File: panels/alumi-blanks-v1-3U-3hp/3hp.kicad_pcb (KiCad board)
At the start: 2 copper layers, 14.9 x 128.5 mm, 2 parts

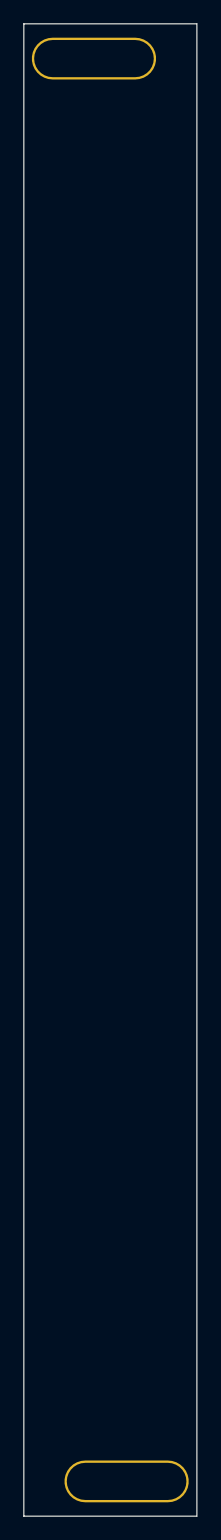
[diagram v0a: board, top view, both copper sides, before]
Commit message: feat: add new screw hole footprints and update panel KiCad files for new JLCPCB order
- Added modular-3M-screw-hole-size1-alumi-0604, modular-3M-screw-hole-size1-fit-alumi-0604, modular-3M-screw-hole-size2-alumi-0604
- Updated all panel .kicad_pcb and .kicad_pro files for 3U panels (1hp-16hp)
- Added new JLCPCB order snapshot and Gerber outputs

Co-authored-by: Copilot <223556219+Copilot@users.noreply.github.com>
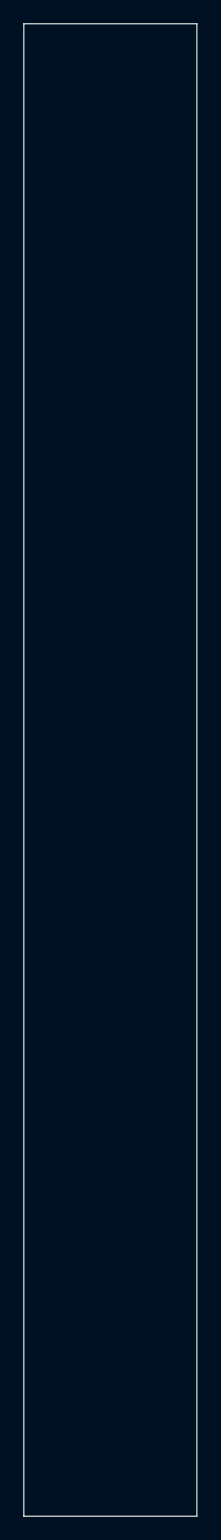
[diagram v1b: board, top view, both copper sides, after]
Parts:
- removed ?: , 
- removed the REF** at (6.04, 3.00)
- added REF**: modular-3M-screw-hole-size2-alumi-0604, zudo-blanks:modular-3M-screw-hole-size2-alumi-0604, F.Cu at (8.86, 125.5)
- added REF**: modular-3M-screw-hole-size2-alumi-0604, zudo-blanks:modular-3M-screw-hole-size2-alumi-0604, F.Cu at (6.04, 3.00)
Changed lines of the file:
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@@
 (kicad_pcb
-	(version 20240108)
+	(version 20260206)
 	(generator "pcbnew")
-	(generator_version "8.0")
+	(generator_version "10.0")
 	(general
 		(thickness 1.6)
@@
 	(layers
 		(0 "F.Cu" signal)
-		(31 "B.Cu" signal)
-		(32 "B.Adhes" user "B.Adhesive")
-		(33 "F.Adhes" user "F.Adhesive")
-		(34 "B.Paste" user)
-		(35 "F.Paste" user)
-		(36 "B.SilkS" user "B.Silkscreen")
-		(37 "F.SilkS" user "F.Silkscreen")
-		(38 "B.Mask" user)
-		(39 "F.Mask" user)
-		(40 "Dwgs.User" user "User.Drawings")
-		(41 "Cmts.User" user "User.Comments")
-		(42 "Eco1.User" user "User.Eco1")
-		(43 "Eco2.User" user "User.Eco2")
-		(44 "Edge.Cuts" user)
-		(45 "Margin" user)
-		(46 "B.CrtYd" user "B.Courtyard")
-		(47 "F.CrtYd" user "F.Courtyard")
-		(48 "B.Fab" user)
-		(49 "F.Fab" user)
-		(50 "User.1" user)
-		(51 "User.2" user)
-		(52 "User.3" user)
-		(53 "User.4" user)
-		(54 "User.5" user)
-		(55 "User.6" user)
-		(56 "User.7" user)
-		(57 "User.8" user)
-		(58 "User.9" user)
+		(2 "B.Cu" signal)
+		(9 "F.Adhes" user "F.Adhesive")
+		(11 "B.Adhes" user "B.Adhesive")
+		(13 "F.Paste" user)
+		(15 "B.Paste" user)
+		(5 "F.SilkS" user "F.Silkscreen")
+		(7 "B.SilkS" user "B.Silkscreen")
+		(1 "F.Mask" user)
+		(3 "B.Mask" user)
+		(17 "Dwgs.User" user "User.Drawings")
+		(19 "Cmts.User" user "User.Comments")
+		(21 "Eco1.User" user "User.Eco1")
+		(23 "Eco2.User" user "User.Eco2")
+		(25 "Edge.Cuts" user)
+		(27 "Margin" user)
+		(31 "F.CrtYd" user "F.Courtyard")
+		(29 "B.CrtYd" user "B.Courtyard")
+		(35 "F.Fab" user)
+		(33 "B.Fab" user)
+		(39 "User.1" user)
+		(41 "User.2" user)
+		(43 "User.3" user)
+		(45 "User.4" user)
+		(47 "User.5" user)
+		(49 "User.6" user)
+		(51 "User.7" user)
+		(53 "User.8" user)
+		(55 "User.9" user)
 	)
 	(setup
 		(pad_to_mask_clearance 0)
 		(allow_soldermask_bridges_in_footprints no)
+		(tenting
+			(front yes)
+			(back yes)
+		)
+		(covering
+			(front no)
+			(back no)
+		)
+		(plugging
+			(front no)
+			(back no)
+		)
+		(capping no)
+		(filling no)
 		(pcbplotparams
-			(layerselection 0x00010fc_ffffffff)
-			(plot_on_all_layers_selection 0x0000000_00000000)
+			(layerselection 0x00000000_00000000_55555555_5755555a)
+			(plot_on_all_layers_selection 0x00000000_00000000_00000000_00000000)
 			(disableapertmacros no)
 			(usegerberextensions no)
@@
 			(usegerberadvancedattributes yes)
 			(creategerberjobfile yes)
-			(dashed_line_dash_ratio 12.000000)
-			(dashed_line_gap_ratio 3.000000)
+			(dashed_line_dash_ratio 12)
+			(dashed_line_gap_ratio 3)
 			(svgprecision 4)
 			(plotframeref no)
-			(viasonmask no)
 			(mode 1)
 			(useauxorigin no)
-			(hpglpennumber 1)
-			(hpglpenspeed 20)
-			(hpglpendiameter 15.000000)
 			(pdf_front_fp_property_popups yes)
 			(pdf_back_fp_property_popups yes)
+			(pdf_metadata yes)
+			(pdf_single_document no)
 			(dxfpolygonmode yes)
 			(dxfimperialunits yes)
@@
 			(psnegative no)
 			(psa4output no)
-			(plotreference yes)
-			(plotvalue yes)
-			(plotfptext yes)
-			(plotinvisibletext no)
+			(plot_black_and_white yes)
 			(sketchpadsonfab no)
+			(plotpadnumbers no)
+			(hidednponfab no)
+			(sketchdnponfab yes)
+			(crossoutdnponfab yes)
 			(subtractmaskfromsilk no)
 			(outputformat 1)
@@
 		)
 	)
-	(net 0 "")
-	(footprint ""
+	(footprint "zudo-blanks:modular-3M-screw-hole-size2-alumi-0604"
 		(layer "F.Cu")
-		(at 8.85 125.5)
-		(property "Reference" ""
-			(at 0 0 0)
-			(layer "F.SilkS")
-			(effects
-				(font
-					(size 1.27 1.27)
-					(thickness 0.15)
-				)
-			)
-		)
-		(property "Value" ""
-			(at 0 0 0)
-			(layer "F.Fab")
-			(effects
-				(font
-					(size 1.27 1.27)
-					(thickness 0.15)
-				)
-			)
-		)
-		(property "Footprint" ""
-			(at 0 0 0)
-			(layer "F.Fab")
-			(hide yes)
-			(effects
-				(font
-					(size 1.27 1.27)
-					(thickness 0.15)
-				)
-			)
-		)
-		(property "Datasheet" ""
-			(at 0 0 0)
-			(layer "F.Fab")
-			(hide yes)
-			(effects
-				(font
-					(size 1.27 1.27)
-					(thickness 0.15)
-				)
-			)
-		)
-		(property "Description" ""
-			(at 0 0 0)
-			(layer "F.Fab")
-			(hide yes)
-			(effects
-				(font
-					(size 1.27 1.27)
-					(thickness 0.15)
-				)
-			)
-		)
-		(pad "1" thru_hole roundrect
-			(at 0 0 90)
-			(size 3.6 10.7)
-			(drill oval 3.2 10.3)
-			(layers "*.Cu" "*.Mask")
-			(remove_unused_layers no)
-			(roundrect_rratio 0.5)
-		)
-	)
-	(footprint "Takazudo:M3-hole-wide-deco"
-		(layer "F.Cu")
-		(at 6.04 3)
+		(at 8.855 125.5)
 		(property "Reference" "REF**"
 			(at 0 -0.5 0)
@@
 			)
 		)
-		(property "Value" "M3-hole-wide-deco"
+		(property "Value" "modular-3M-screw-hole-size2-alumi-0604"
 			(at 0 1 0)
 			(unlocked yes)
@@
 			)
 		)
-		(property "Footprint" "Takazudo:M3-hole-wide-deco"
-			(at 0 0 0)
-			(unlocked yes)
-			(layer "F.Fab")
-			(hide yes)
-			(effects
-				(font
-					(size 1 1)
-					(thickness 0.15)
-				)
-			)
-		)
 		(property "Datasheet" ""
 			(at 0 0 0)
@@
 			)
 		)
-		(attr through_hole)
-		(pad "1" thru_hole roundrect
+		(attr smd)
+		(duplicate_pad_numbers_are_jumpers no)
+		(pad "" np_thru_hole roundrect
 			(at 0 0 90)
-			(size 3.6 10.7)
-			(drill oval 3.2 10.3)
-			(layers "*.Cu" "*.Mask")
-			(remove_unused_layers no)
-			(roundrect_rratio 0.5)
-		)
-	)
-	(gr_poly
-		(pts
-			(xy 14.900195 128.494736) (xy 0.000001 128.494736) (xy 0.000001 0.005265) (xy 14.900195 0.005265)
-		)
+			(size 4 11.08)
+			(drill oval 3.2 10.28)
+			(layers "*.Mask")
+			(roundrect_rratio 0.4998750312)
+		)
+		(embedded_fonts no)
+	)
+	(footprint "zudo-blanks:modular-3M-screw-hole-size2-alumi-0604"
+		(layer "F.Cu")
+		(at 6.045 3)
+		(property "Reference" "REF**"
+			(at 0 -0.5 0)
+			(unlocked yes)
+			(layer "F.SilkS")
+			(hide yes)
+			(effects
+				(font
+					(size 1 1)
+					(thickness 0.1)
+				)
+			)
+		)
+		(property "Value" "modular-3M-screw-hole-size2-alumi-0604"
+			(at 0 1 0)
+			(unlocked yes)
+			(layer "F.Fab")
+			(hide yes)
+			(effects
+				(font
+					(size 1 1)
+					(thickness 0.15)
+				)
+			)
+		)
+		(property "Datasheet" ""
+			(at 0 0 0)
+			(unlocked yes)
+			(layer "F.Fab")
+			(hide yes)
+			(effects
+				(font
+					(size 1 1)
+					(thickness 0.15)
+				)
+			)
+		)
+		(property "Description" ""
+			(at 0 0 0)
+			(unlocked yes)
+			(layer "F.Fab")
+			(hide yes)
+			(effects
+				(font
+					(size 1 1)
+					(thickness 0.15)
+				)
+			)
+		)
+		(attr smd)
+		(duplicate_pad_numbers_are_jumpers no)
+		(pad "" np_thru_hole roundrect
+			(at 0 0 90)
+			(size 4 11.08)
+			(drill oval 3.2 10.28)
+			(layers "*.Mask")
+			(roundrect_rratio 0.4998750312)
+		)
+		(embedded_fonts no)
+	)
+	(gr_rect
+		(start 0 0)
+		(end 14.9 128.5)
 		(stroke
-			(width 0.1)
+			(width 0.05)
 			(type solid)
 		)
-		(fill solid)
+		(fill no)
 		(layer "Edge.Cuts")
 	)
-	(gr_poly
-		(pts
-			(xy 13.503301 1.204617) (xy 0.000001 1.204617) (xy 0.000001 0.005265) (xy 13.503301 0.005265)
-		)
-		(stroke
-			(width -0.000001)
-			(type solid)
-		)
-		(fill solid)
-		(layer "User.1")
-	)
-	(gr_poly
-		(pts
-			(xy 0.698448 30.003191) (xy 0.000001 30.003191) (xy 0.000001 0.005265) (xy 0.698448 0.005265)
-		)
-		(stroke
-			(width -0.000001)
-			(type solid)
-		)
-		(fill solid)
-		(layer "User.1")
-	)
-	(gr_poly
-		(pts
-			(xy 14.900206 128.49472) (xy 1.396906 128.49472) (xy 1.396906 127.295372) (xy 14.900206 127.295372)
-		)
-		(stroke
-			(width -0.000001)
-			(type solid)
-		)
-		(fill solid)
-		(layer "User.1")
-	)
-	(gr_poly
-		(pts
-			(xy 14.900202 128.494751) (xy 14.201756 128.494751) (xy 14.201757 98.496819) (xy 14.900205 98.496819)
-		)
-		(stroke
-			(width -0.000001)
-			(type solid)
-		)
-		(fill solid)
-		(layer "User.1")
-	)
+	(embedded_fonts no)
 )
